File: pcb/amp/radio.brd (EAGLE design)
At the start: 34.3 x 44.5 mm, 13 parts, among them IC1 LM1117S, U1 TEA5767

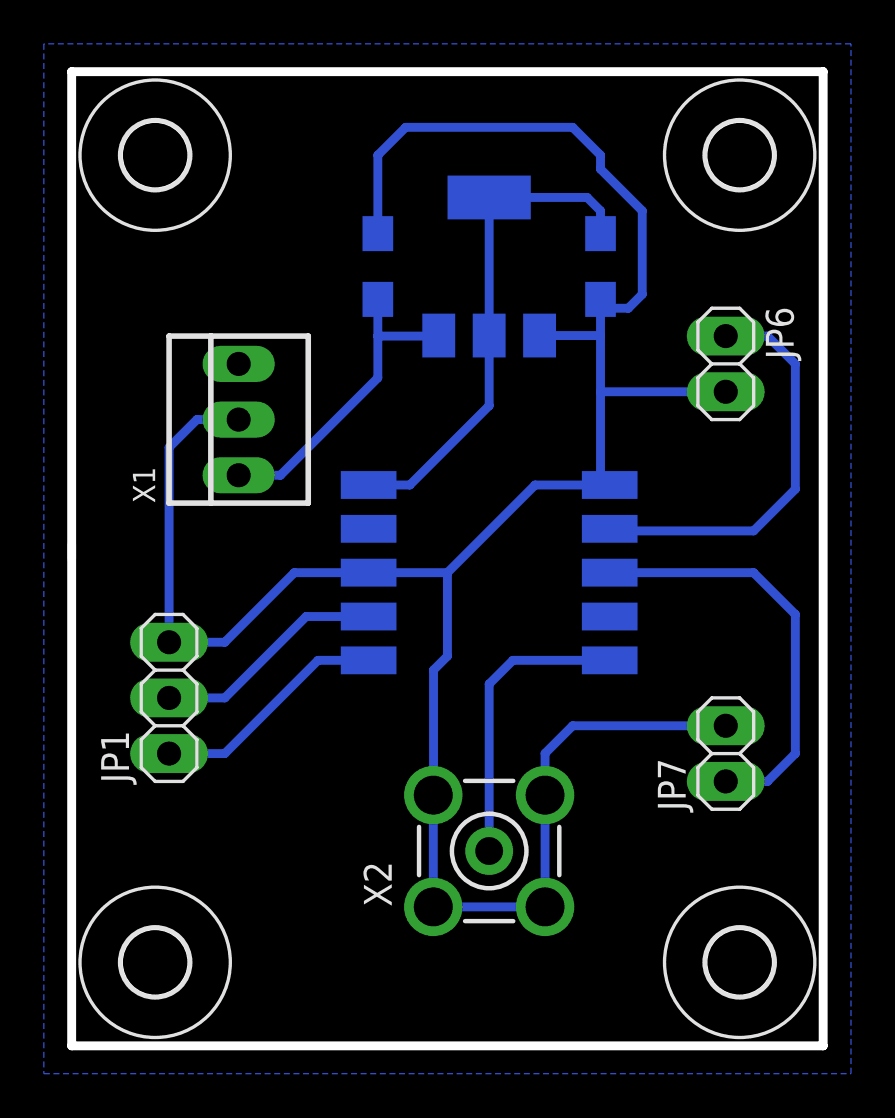
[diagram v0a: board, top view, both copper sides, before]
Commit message: 
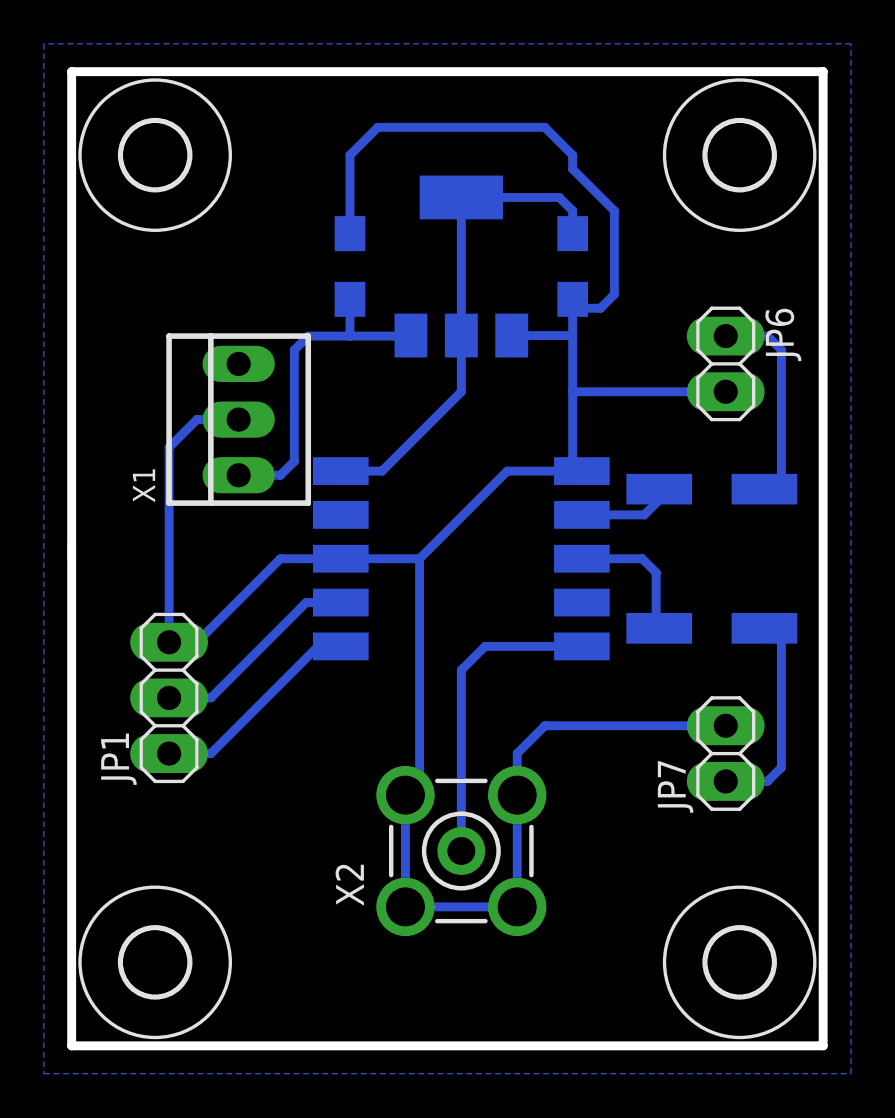
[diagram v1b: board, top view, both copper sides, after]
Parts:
- added C3, C4: (no value), amp:PANASONIC_D
- C1, C2: value (none) -> 10uF
- moved U1 1.42 mm to (17.8, 22.2)
- moved C1 1.27 mm to (12.7, 35.6)
- moved C2 1.27 mm to (22.9, 35.6)
- moved IC1 1.27 mm to (17.8, 35.6)
- moved X2 1.27 mm to (17.8, 8.89)
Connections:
- removed net OUT_L: JP6.1, U1.7
- new net N$2: C3.+, U1.7
- new net N$3: C3.-, JP6.1
- new net N$4: C4.-, JP7.1
- net OUT_R: now also C4.+; no longer JP7.1
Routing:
- net OUT_L: track 18.7 -> 0.00 mm
- net OUT_R: track 19.3 -> 6.25 mm
- net N$3: track 0.00 -> 9.93 mm
- net N$4: track 0.00 -> 9.56 mm
- net N$2: track 0.00 -> 4.51 mm
- net GND: track 113.5 -> 115.0 mm
- net SCL: track 10.6 -> 9.64 mm
- net SDA: track 10.9 -> 9.86 mm
- net N$1: track 13.6 -> 14.2 mm
- net +3V3: track 22.9 -> 22.2 mm
- net +12V: track 14.6 -> 15.2 mm

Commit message: 
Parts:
- C1, C2: value 10uF -> 1uF
- C3, C4: value (none) -> 22uF
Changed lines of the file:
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@@
 <?xml version="1.0" encoding="utf-8"?>
 <!DOCTYPE eagle SYSTEM "eagle.dtd">
-<eagle version="6.1">
+<eagle version="6.4">
 <drawing>
 <settings>
@@
 </class>
 </classes>
-<designrules>
+<designrules name="default">
 <description language="de">&lt;b&gt;EAGLE Design Rules&lt;/b&gt;
 &lt;p&gt;
@@
 <element name="IC1" library="amp" package="SOT223" value="LM1117S" x="17.78" y="35.56" rot="MR0"/>
 <element name="JP1" library="amp" package="1X03" value="" x="4.445" y="15.875" rot="R90"/>
-<element name="C1" library="amp" package="SMC_A" value="10uF" x="12.7" y="35.56" rot="MR90"/>
-<element name="C2" library="amp" package="SMC_A" value="10uF" x="22.86" y="35.56" rot="MR270"/>
+<element name="C1" library="amp" package="SMC_A" value="1uF" x="12.7" y="35.56" rot="MR90"/>
+<element name="C2" library="amp" package="SMC_A" value="1uF" x="22.86" y="35.56" rot="MR270"/>
 <element name="X2" library="amp" package="BU-SMA-V" value="" x="17.78" y="8.89" rot="R90">
 <attribute name="OC_NEWARK" value="unknown" x="17.78" y="8.89" size="1.778" layer="27" font="vector" ratio="15" rot="R90" display="off"/>
@@
 <attribute name="OC_FARNELL" value="unknown" x="17.78" y="8.89" size="1.778" layer="27" font="vector" ratio="15" rot="R90" display="off"/>
 </element>
-<element name="C3" library="amp" package="PANASONIC_D" value="" x="29.21" y="25.4" rot="MR0"/>
-<element name="C4" library="amp" package="PANASONIC_D" value="" x="29.21" y="19.05" rot="MR0"/>
+<element name="C3" library="amp" package="PANASONIC_D" value="22uF" x="29.21" y="25.4" rot="MR0"/>
+<element name="C4" library="amp" package="PANASONIC_D" value="22uF" x="29.21" y="19.05" rot="MR0"/>
 </elements>
 <signals>
